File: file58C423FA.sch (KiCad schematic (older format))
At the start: 53 parts

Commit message: Schematic complete
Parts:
- added D5, D6, D7, D8: TL4050B51, TO_SOT_Packages_SMD:SOT-23, symbol TL4050B51
- added R23, R24: 750, Resistors_SMD:R_0603_HandSoldering, symbol R
- added R45: 3.3k, Resistors_SMD:R_0603_HandSoldering, symbol R
- R29: renamed from R?; value 1k -> 10k
- gave numbers to parts that had none: 46
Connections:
- net +15V: now also R23.1, R45.1
- net -15V: now also R24.2
- net 10V: now also D7.1 (K), R45.2; no longer RV4.3
- net GND: now also P3.4, P4.4, U6.10 (+), U7.5 (+), D5.2 (A), D6.1 (K), D8.2 (A); no longer P3.2, P4.2, RV4.1, U6.3 (+), U7.3 (+)
- net set_point: now also C21.1, C22.1, R26.1, RV4.2
- net at P3.1, R27.2: now also S4.1; no longer U6.3 (+)
- net at R41.2, S5.1: now also U6.8; no longer U6.1
- net at R39.2, R41.1: now also U6.9 (-); no longer U6.2 (-)
- net at R43.2, S6.1: now also U6.14; no longer U6.1
- net at R40.2, R43.1: now also U6.13 (-); no longer U6.2 (-)
- net at C27.1, C32.1, RV6.2: now also U6.12 (+); no longer U6.3 (+)
- net at R38.2, U9.1, U9.2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: now also U7.6 (-); no longer U7.2 (-)
- net at R25.1: now also P3.3; no longer P3.1
- net at S4.2: now also U6.5 (+); no longer P4.1
- net at R39.1, R42.1, S5.3: now also U7.7; no longer U7.1
- new net: P4.3, U6.6 (-), U6.7
- new net: D6.2 (A), R24.1, RV4.1
- new net: D5.1 (K), R23.2, RV4.3
- new net: D7.2 (A), D8.1 (K)
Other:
- note added: "Note: Set Point voltage is divided by 10 is added to Servo Input,\nsince for path length stabilization we expect to lock very close to the zero point."
- moved on the sheet: C21, C22, C25, C26, RV4, S4

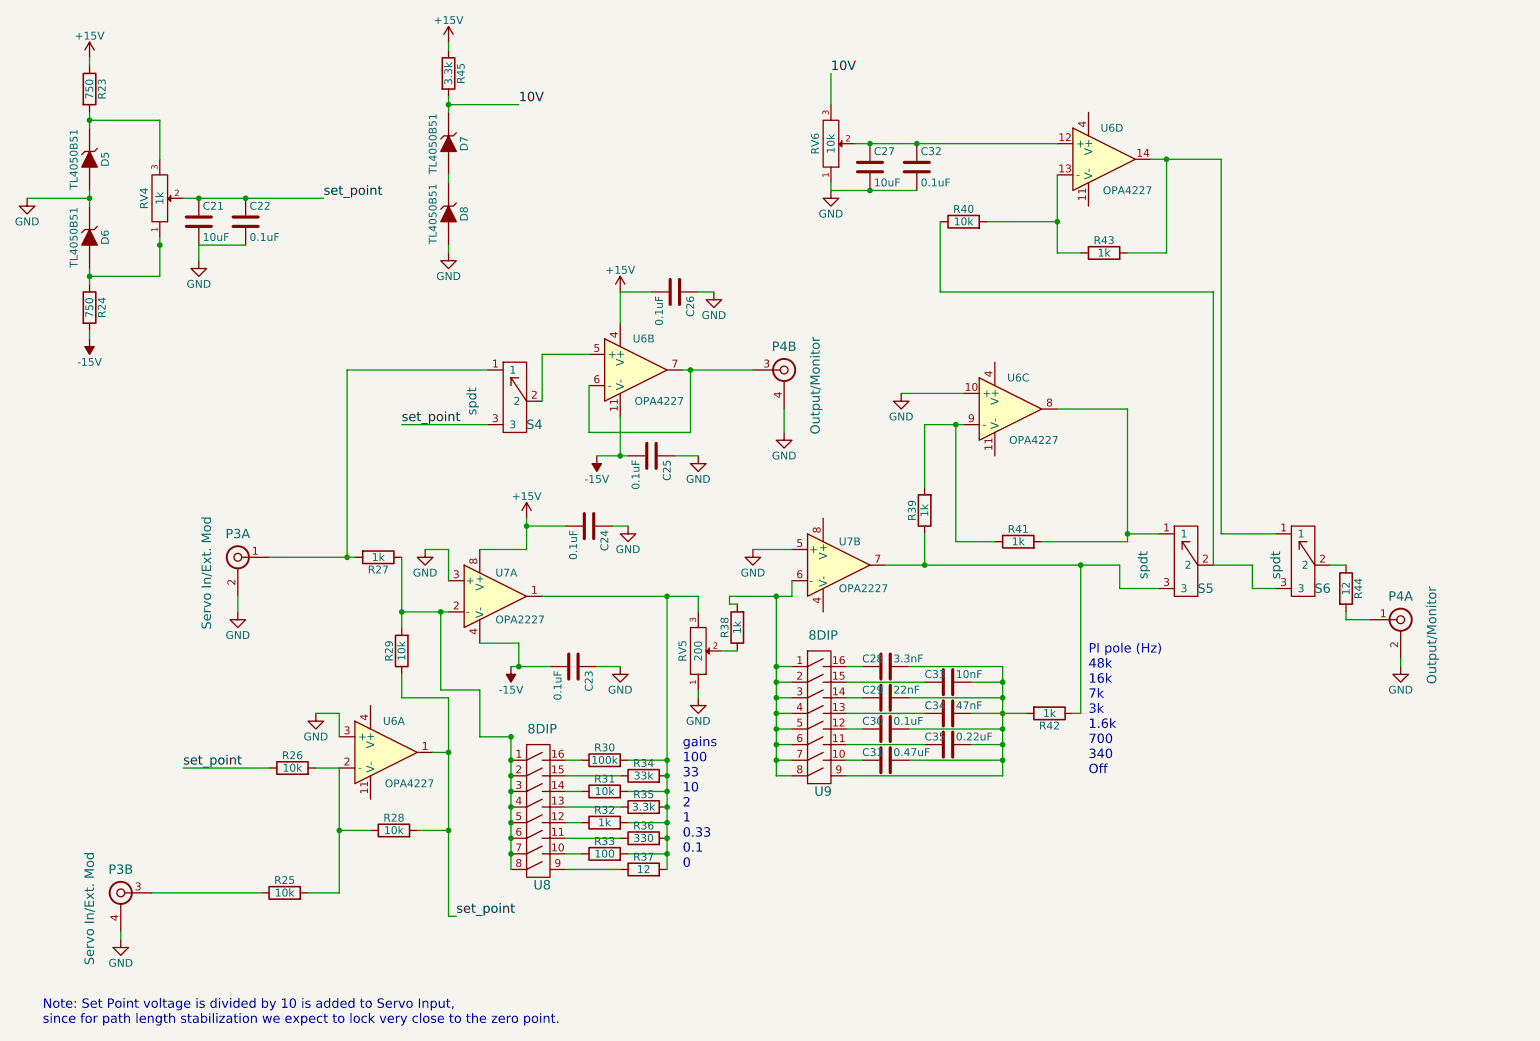
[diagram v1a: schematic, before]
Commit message: Made both circiuts identical
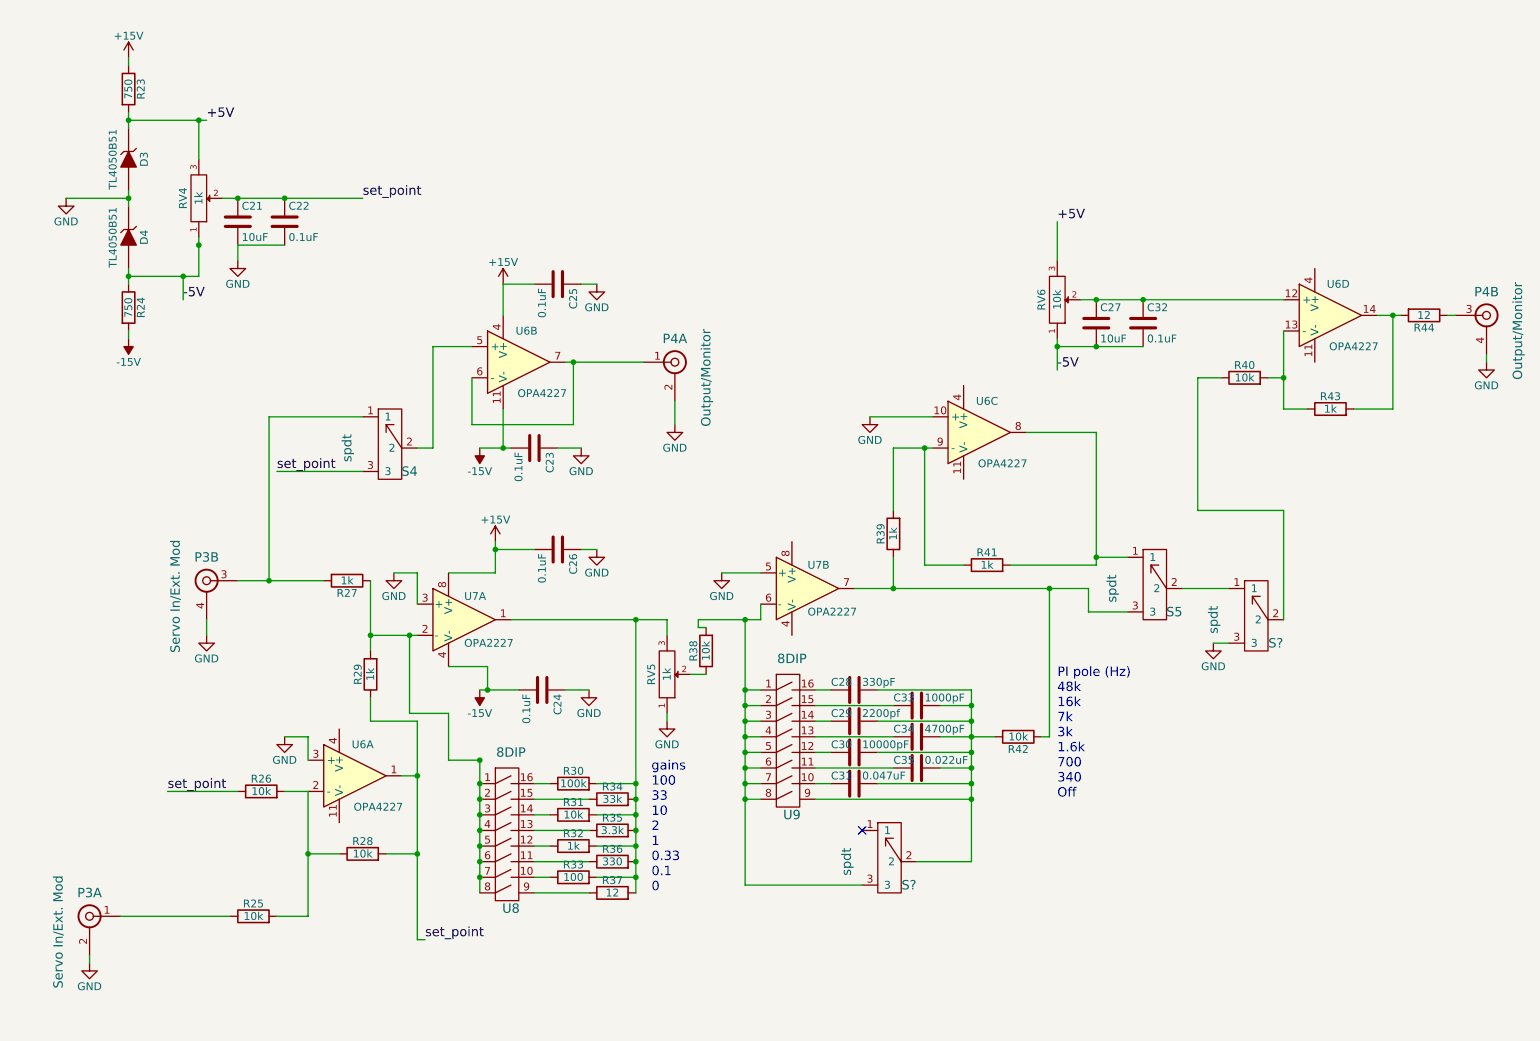
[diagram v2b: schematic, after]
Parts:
- removed D5, D6, D7, D8: TL4050B51, TO_SOT_Packages_SMD:SOT-23, symbol TL4050B51
- removed R45: 3.3k, Resistors_SMD:R_0603_HandSoldering, symbol R
- removed S6: spdt, footprints:CJS-1200TB-SPDT, symbol spdt
- added D3, D4: TL4050B51, symbol TL4050B51
- added S? (x2): spdt, symbol spdt
- C21, C22, C23, C24, C25, C26, C27, C32: footprint Capacitors_SMD:C_0603_HandSoldering -> (none)
- C28: value 3.3nF -> 330pF; footprint Capacitors_SMD:C_0603_HandSoldering -> (none)
- C29: value 22nF -> 2200pf; footprint Capacitors_SMD:C_0603_HandSoldering -> (none)
- C30: value 0.1uF -> 10000pF; footprint Capacitors_SMD:C_0603_HandSoldering -> (none)
- C31: value 0.47uF -> 0.047uF; footprint Capacitors_SMD:C_0603_HandSoldering -> (none)
- C33: value 10nF -> 1000pF; footprint Capacitors_SMD:C_0603_HandSoldering -> (none)
- C34: value 47nF -> 4700pF; footprint Capacitors_SMD:C_0603_HandSoldering -> (none)
- C35: value 0.22uF -> 0.022uF; footprint Capacitors_SMD:C_0603_HandSoldering -> (none)
- P4: footprint footprints:Dual-BNC-ARF2136 -> (none)
- R23, R24, R25, R26, R27, R28, R30, R31, R32, R33, R34, R35, R36, R37, R39, R40, R41, R43, R44: footprint Resistors_SMD:R_0603_HandSoldering -> (none)
- R29: value 10k -> 1k; footprint Resistors_SMD:R_0603_HandSoldering -> (none)
- R38, R42: value 1k -> 10k; footprint Resistors_SMD:R_0603_HandSoldering -> (none)
- RV4: footprint footprints:VishaySpectrol536 -> (none)
- RV5: value 200 -> 1k
- RV6: footprint footprints:Bourns-PV36W104C01B00-trimmer -> (none)
- S4, S5: footprint footprints:CJS-1200TB-SPDT -> (none)
- U6: footprint Housings_SOIC:SOIC-14_3.9x8.7mm_Pitch1.27mm -> (none)
- U7: footprint Housings_SOIC:SOIC-8_3.9x4.9mm_Pitch1.27mm -> (none)
- U8, U9: footprint footprints:8_POS_DIP_Switch -> (none)
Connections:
- net 10V is gone; now on net +5V: RV6.3
- net +15V: now also C25.2; no longer C24.2
- net -15V: now also C24.2; no longer C25.2
- net GND: now also D3.2 (A), D4.1 (K), S?.3; no longer C27.2, C32.2, RV6.1
- net at U6.6 (-), U6.7: now also P4.1; no longer P4.3
- net at R43.2, U6.14: now also R44.2
- net -5V: now reaches R24.1, RV4.1
- net -5V: now also C27.2, C32.2, RV6.1, D4.2 (A)
- net +5V: now reaches R23.2, RV4.3
- net +5V: now also D3.1 (K)
- net at R27.2, S4.1: now also P3.3; no longer P3.1
- net at R38.2, U7.6 (-), U9.1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: now also S?.3
- net at C28.1, C29.1, C30.1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: now also S?.2
- net at R25.1: now also P3.1; no longer P3.3
- net at S5.2: now also S?.1; no longer R40.1
- net at R44.1: now also P4.3
- new net: R40.1, S?.2
- no-connect marks 0 -> 1
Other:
- note removed: "Note: Set Point voltage is divided by 10 is added to Servo Input,\nsince for path length stabilization we expect to lock very close to the zero point."

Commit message: Footprints assigned
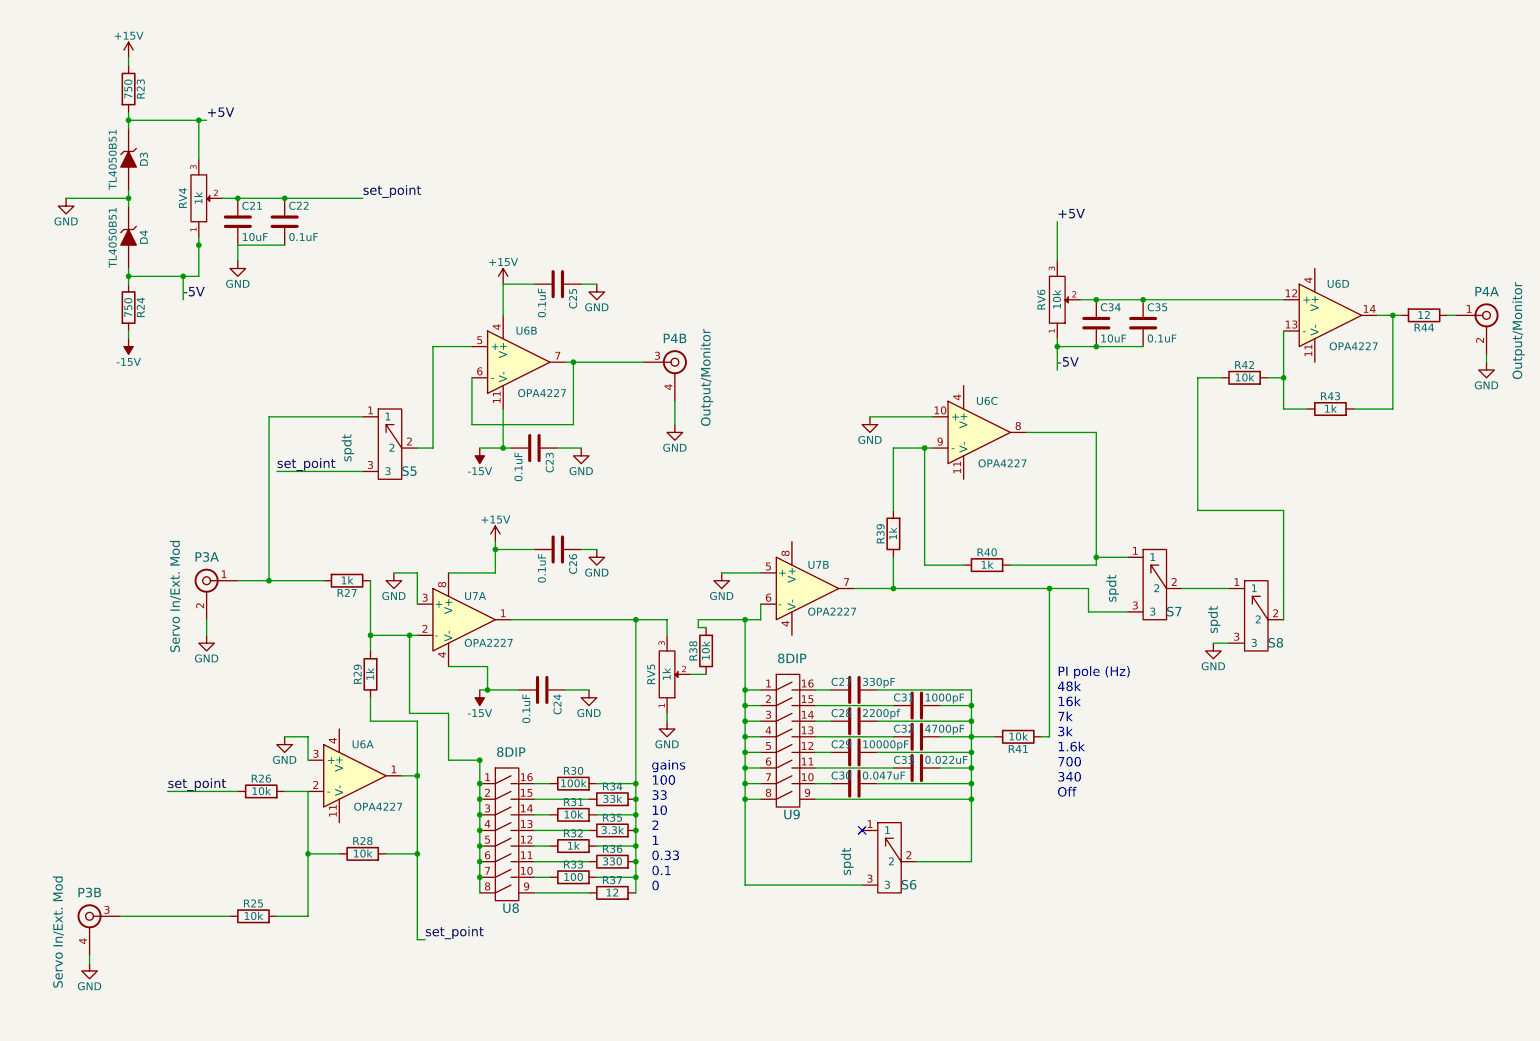
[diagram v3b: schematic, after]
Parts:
- gave numbers to parts that had none: 2
- renumbered C28 to C27, C29 to C28, C30 to C29, C31 to C30, C33 to C31, C34 to C32, C35 to C33, C27 to C34, C32 to C35, R41 to R40, R42 to R41, R40 to R42, S4 to S5, S5 to S7
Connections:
- net at U6.6 (-), U6.7: now also P4.3; no longer P4.1
- net at R27.2, S5.1: now also P3.1; no longer P3.3
- net at R44.1: now also P4.1; no longer P4.3
- net at R25.1: now also P3.3; no longer P3.1
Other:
- moved on the sheet: P3A, P3B, P4A, P4B
